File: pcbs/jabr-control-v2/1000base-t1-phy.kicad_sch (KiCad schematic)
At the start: 28 parts, among them J701 MSPE-J2L0-x00, U701 LAN8870, Y701 XRCGB25M000F3A16R0

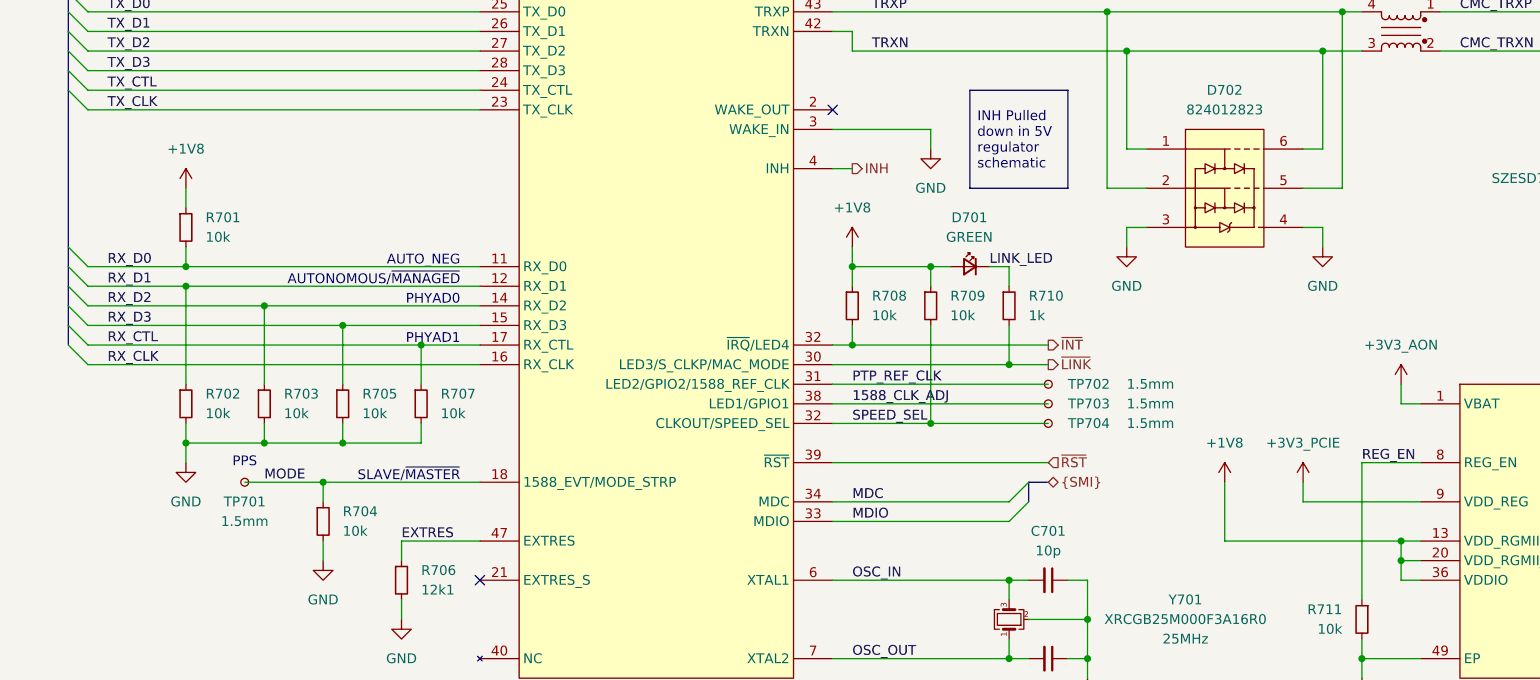
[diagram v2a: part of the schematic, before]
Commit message: PCI11010 IO done
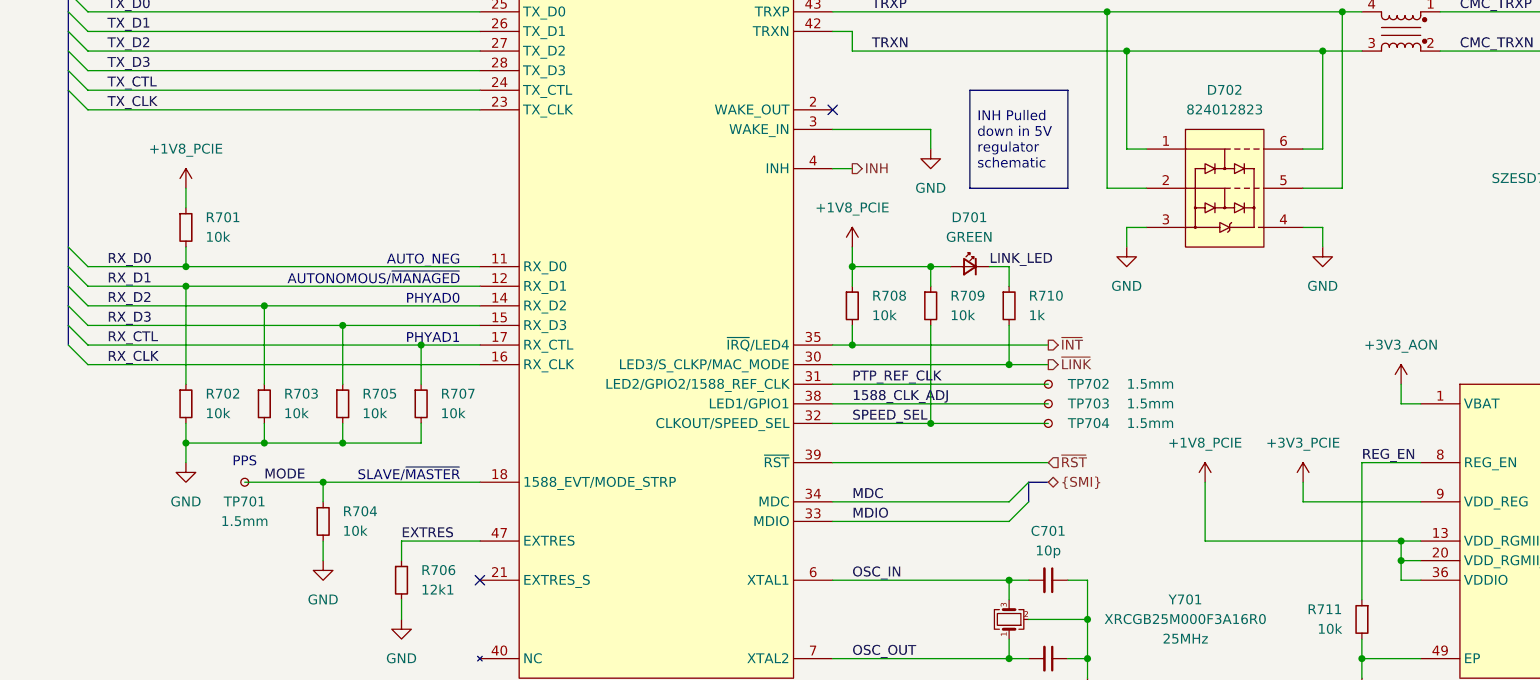
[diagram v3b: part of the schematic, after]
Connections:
- net ~{INT}: now also U701.35 (~{IRQ}/LED4); no longer U701.32 (CLKOUT/SPEED_SEL)
- net +1V8 renamed +1V8_PCIE
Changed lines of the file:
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@@
 	(wire
 		(pts
-			(xy 177.8 121.92) (xy 200.66 121.92)
+			(xy 175.26 121.92) (xy 200.66 121.92)
 		)
 		(stroke
@@
 	(wire
 		(pts
-			(xy 177.8 114.3) (xy 177.8 121.92)
+			(xy 175.26 114.3) (xy 175.26 121.92)
 		)
 		(stroke
@@
 	)
 	(symbol
+		(lib_id "PWR-SYM:+1V8_PCIE")
+		(at 43.18 76.2 0)
+		(unit 1)
+		(body_style 1)
+		(exclude_from_sim no)
+		(in_bom yes)
+		(on_board yes)
+		(in_pos_files yes)
+		(dnp no)
+		(fields_autoplaced yes)
+		(property "Reference" "#PWR0718"
+			(at 43.18 80.01 0)
+			(hide yes)
+			(show_name no)
+			(do_not_autoplace no)
+			(effects
+				(font
+					(size 1.27 1.27)
+				)
+			)
+		)
+		(property "Value" "+1V8_PCIE"
+			(at 43.18 71.12 0)
+			(show_name no)
+			(do_not_autoplace no)
+			(effects
+				(font
+					(size 1.27 1.27)
+				)
+			)
+		)
+		(property "Footprint" ""
+			(at 43.18 76.2 0)
+			(hide yes)
+			(show_name no)
+			(do_not_autoplace no)
+			(effects
+				(font
+					(size 1.27 1.27)
+				)
+			)
+		)
+		(property "Datasheet" ""
+			(at 43.18 76.2 0)
+			(hide yes)
+			(show_name no)
+			(do_not_autoplace no)
+			(effects
+				(font
+					(size 1.27 1.27)
+				)
+			)
+		)
+		(property "Description" "Power symbol creates a global label with name \"+1V8_PCIE\""
+			(at 43.18 76.2 0)
+			(hide yes)
+			(show_name no)
+			(do_not_autoplace no)
+			(effects
+				(font
+					(size 1.27 1.27)
+				)
+			)
+		)
+		(pin "1"
+		)
+		(instances
+			(project "jabr-control-v2"
+				(path "/f91ec272-d09a-4038-bbbb-962739a92c51/760d12ad-9269-4cb7-9058-d98dd001df15"
+					(reference "#PWR0718")
+					(unit 1)
+				)
+			)
+		)
+	)
+	(symbol
 		(lib_id "COMM-CMC:ACT1210G-800-2P-TL10")
 		(at 200.66 53.34 0)
@@
 	)
 	(symbol
-		(lib_id "power:+1V8")
-		(at 177.8 114.3 0)
-		(unit 1)
-		(body_style 1)
-		(exclude_from_sim no)
-		(in_bom yes)
-		(on_board yes)
-		(in_pos_files yes)
-		(dnp no)
-		(fields_autoplaced yes)
-		(property "Reference" "#PWR0709"
-			(at 177.8 118.11 0)
-			(hide yes)
-			(show_name no)
-			(do_not_autoplace no)
-			(effects
-				(font
-					(size 1.27 1.27)
-				)
-			)
-		)
-		(property "Value" "+1V8"
-			(at 177.8 109.22 0)
-			(show_name no)
-			(do_not_autoplace no)
-			(effects
-				(font
-					(size 1.27 1.27)
-				)
-			)
-		)
-		(property "Footprint" ""
-			(at 177.8 114.3 0)
-			(hide yes)
-			(show_name no)
-			(do_not_autoplace no)
-			(effects
-				(font
-					(size 1.27 1.27)
-				)
-			)
-		)
-		(property "Datasheet" ""
-			(at 177.8 114.3 0)
-			(hide yes)
-			(show_name no)
-			(do_not_autoplace no)
-			(effects
-				(font
-					(size 1.27 1.27)
-				)
-			)
-		)
-		(property "Description" "Power symbol creates a global label with name \"+1V8\""
-			(at 177.8 114.3 0)
-			(hide yes)
-			(show_name no)
-			(do_not_autoplace no)
-			(effects
-				(font
-					(size 1.27 1.27)
-				)
-			)
-		)
-		(pin "1"
-		)
-		(instances
-			(project "jabr-control-v2"
-				(path "/f91ec272-d09a-4038-bbbb-962739a92c51/760d12ad-9269-4cb7-9058-d98dd001df15"
-					(reference "#PWR0709")
-					(unit 1)
-				)
-			)
-		)
-	)
-	(symbol
 		(lib_id "DEV:R_SMALL")
 		(at 139.7 91.44 0)
@@
 	)
 	(symbol
-		(lib_id "power:+1V8")
-		(at 129.54 83.82 0)
-		(unit 1)
-		(body_style 1)
-		(exclude_from_sim no)
-		(in_bom yes)
-		(on_board yes)
-		(in_pos_files yes)
-		(dnp no)
-		(fields_autoplaced yes)
-		(property "Reference" "#PWR0705"
-			(at 129.54 87.63 0)
-			(hide yes)
-			(show_name no)
-			(do_not_autoplace no)
-			(effects
-				(font
-					(size 1.27 1.27)
-				)
-			)
-		)
-		(property "Value" "+1V8"
-			(at 129.54 78.74 0)
-			(show_name no)
-			(do_not_autoplace no)
-			(effects
-				(font
-					(size 1.27 1.27)
-				)
-			)
-		)
-		(property "Footprint" ""
-			(at 129.54 83.82 0)
-			(hide yes)
-			(show_name no)
-			(do_not_autoplace no)
-			(effects
-				(font
-					(size 1.27 1.27)
-				)
-			)
-		)
-		(property "Datasheet" ""
-			(at 129.54 83.82 0)
-			(hide yes)
-			(show_name no)
-			(do_not_autoplace no)
-			(effects
-				(font
-					(size 1.27 1.27)
-				)
-			)
-		)
-		(property "Description" "Power symbol creates a global label with name \"+1V8\""
-			(at 129.54 83.82 0)
-			(hide yes)
-			(show_name no)
-			(do_not_autoplace no)
-			(effects
-				(font
-					(size 1.27 1.27)
-				)
-			)
-		)
-		(pin "1"
-		)
-		(instances
-			(project "jabr-control-v2"
-				(path "/f91ec272-d09a-4038-bbbb-962739a92c51/760d12ad-9269-4cb7-9058-d98dd001df15"
-					(reference "#PWR0705")
-					(unit 1)
-				)
-			)
-		)
-	)
-	(symbol
 		(lib_id "power:GND")
 		(at 160.02 139.7 0)
@@
 	)
 	(symbol
-		(lib_id "power:+1V8")
-		(at 43.18 76.2 0)
+		(lib_id "PWR-SYM:+1V8_PCIE")
+		(at 129.54 83.82 0)
 		(unit 1)
 		(body_style 1)
@@
 		(dnp no)
 		(fields_autoplaced yes)
-		(property "Reference" "#PWR0701"
-			(at 43.18 80.01 0)
+		(property "Reference" "#PWR0716"
+			(at 129.54 87.63 0)
 			(hide yes)
 			(show_name no)
@@
 			)
 		)
-		(property "Value" "+1V8"
-			(at 43.18 71.12 0)
+		(property "Value" "+1V8_PCIE"
+			(at 129.54 78.74 0)
 			(show_name no)
 			(do_not_autoplace no)
@@
 		)
 		(property "Footprint" ""
-			(at 43.18 76.2 0)
+			(at 129.54 83.82 0)
 			(hide yes)
 			(show_name no)
@@
 		)
 		(property "Datasheet" ""
-			(at 43.18 76.2 0)
+			(at 129.54 83.82 0)
 			(hide yes)
 			(show_name no)
@@
 			)
 		)
-		(property "Description" "Power symbol creates a global label with name \"+1V8\""
-			(at 43.18 76.2 0)
+		(property "Description" "Power symbol creates a global label with name \"+1V8_PCIE\""
+			(at 129.54 83.82 0)
 			(hide yes)
 			(show_name no)
@@
 			(project "jabr-control-v2"
 				(path "/f91ec272-d09a-4038-bbbb-962739a92c51/760d12ad-9269-4cb7-9058-d98dd001df15"
-					(reference "#PWR0701")
+					(reference "#PWR0716")
 					(unit 1)
 				)
@@
 		)
 		(property "Footprint" "project_footprints:lan8870"
-			(at 104.14 149.86 0)
+			(at 104.14 142.24 0)
 			(hide yes)
 			(show_name no)
@@
 		)
 		(property "Datasheet" "https://ww1.microchip.com/downloads/aemDocuments/documents/UNG/ProductDocuments/ProductBrief/LAN8870-LAN8871-LAN8872-Product-Brief-DS00004469.pdf"
-			(at 104.14 157.48 0)
+			(at 104.14 149.86 0)
 			(hide yes)
 			(show_name no)
@@
 		)
 		(property "Description" "100/1000BASE-T1 PHY"
-			(at 104.14 153.67 0)
+			(at 104.14 146.05 0)
 			(hide yes)
 			(show_name no)
@@
 		(pin "32"
 		)
-		(pin "32"
+		(pin "35"
 		)
 		(pin "34"
@@
 					(unit 1)
 				)
+			)
+		)
+	)
+	(symbol
+		(lib_id "PWR-SYM:+1V8_PCIE")
+		(at 175.26 114.3 0)
+		(unit 1)
+		(body_style 1)
+		(exclude_from_sim no)
+		(in_bom yes)
+		(on_board yes)
+		(in_pos_files yes)
+		(dnp no)
+		(fields_autoplaced yes)
+		(property "Reference" "#PWR0721"
+			(at 175.26 118.11 0)
+			(hide yes)
+			(show_name no)
+			(do_not_autoplace no)
+			(effects
+				(font
+					(size 1.27 1.27)
+				)
+			)
+		)
+		(property "Value" "+1V8_PCIE"
+			(at 175.26 109.22 0)
+			(show_name no)
+			(do_not_autoplace no)
+			(effects
+				(font
+					(size 1.27 1.27)
+				)
+			)
+		)
+		(property "Footprint" ""
+			(at 175.26 114.3 0)
+			(hide yes)
+			(show_name no)
+			(do_not_autoplace no)
+			(effects
+				(font
+					(size 1.27 1.27)
+				)
+			)
+		)
+		(property "Datasheet" ""
+			(at 175.26 114.3 0)
+			(hide yes)
+			(show_name no)
+			(do_not_autoplace no)
+			(effects
+				(font
+					(size 1.27 1.27)
+				)
+			)
+		)
+		(property "Description" "Power symbol creates a global label with name \"+1V8_PCIE\""
+			(at 175.26 114.3 0)
+			(hide yes)
+			(show_name no)
+			(do_not_autoplace no)
+			(effects
+				(font
+					(size 1.27 1.27)
+				)
+			)
+		)
+		(pin "1"
+		)
+		(instances
+			(project "jabr-control-v2"
+				(path "/f91ec272-d09a-4038-bbbb-962739a92c51/760d12ad-9269-4cb7-9058-d98dd001df15"
+					(reference "#PWR0721")
+					(unit 1)
+				)

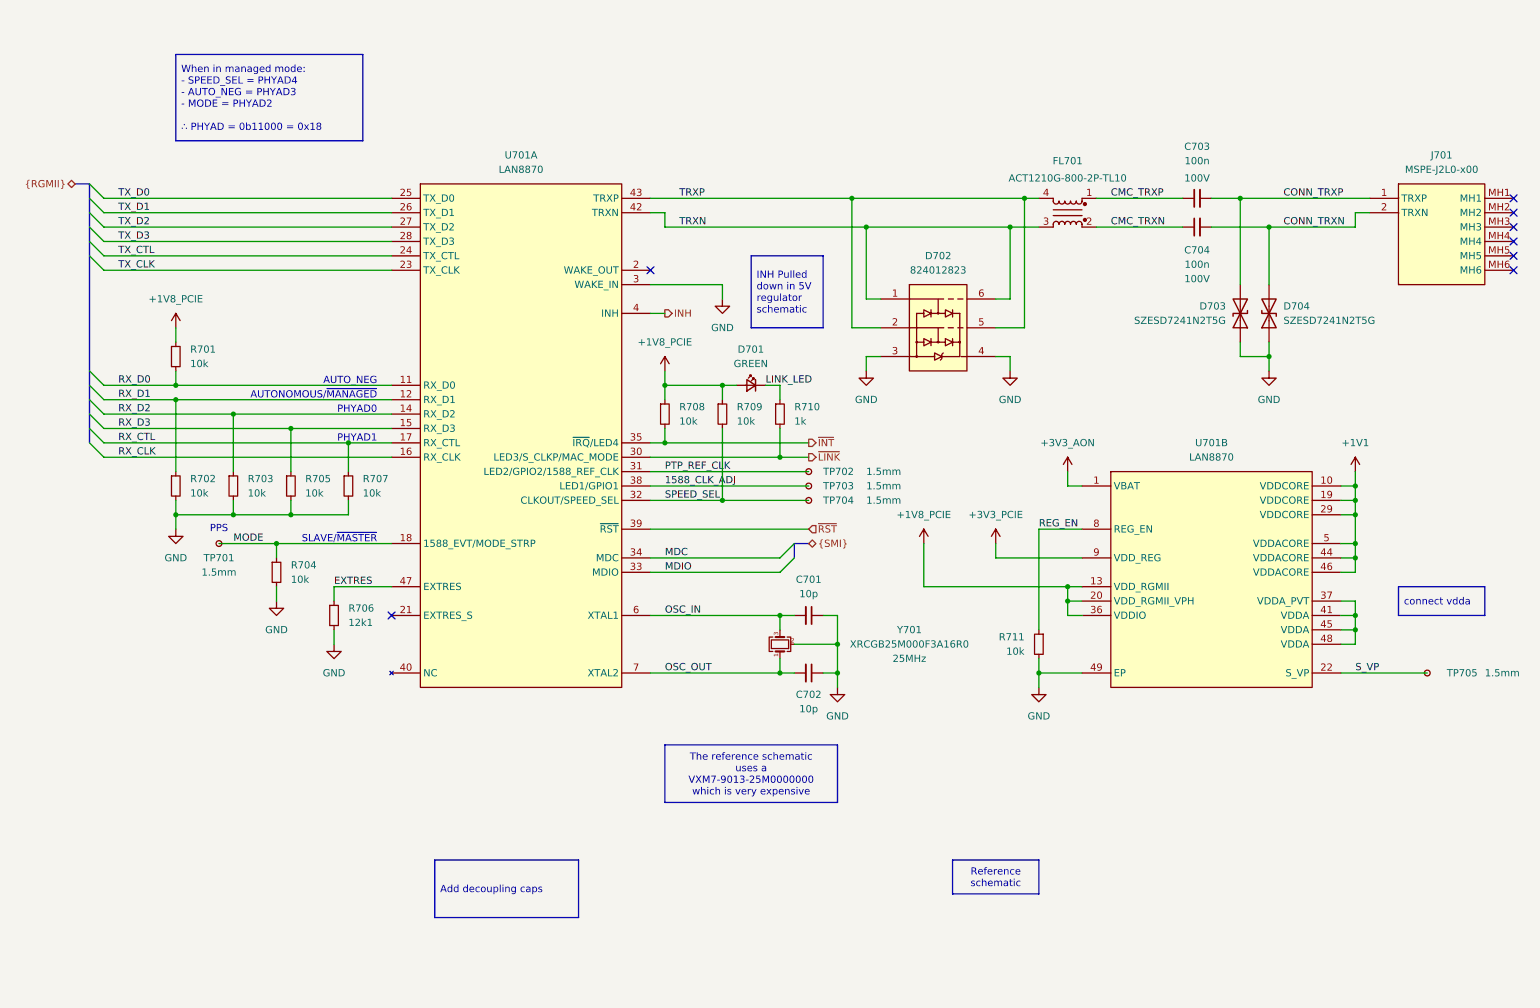
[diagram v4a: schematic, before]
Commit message: Schematic done
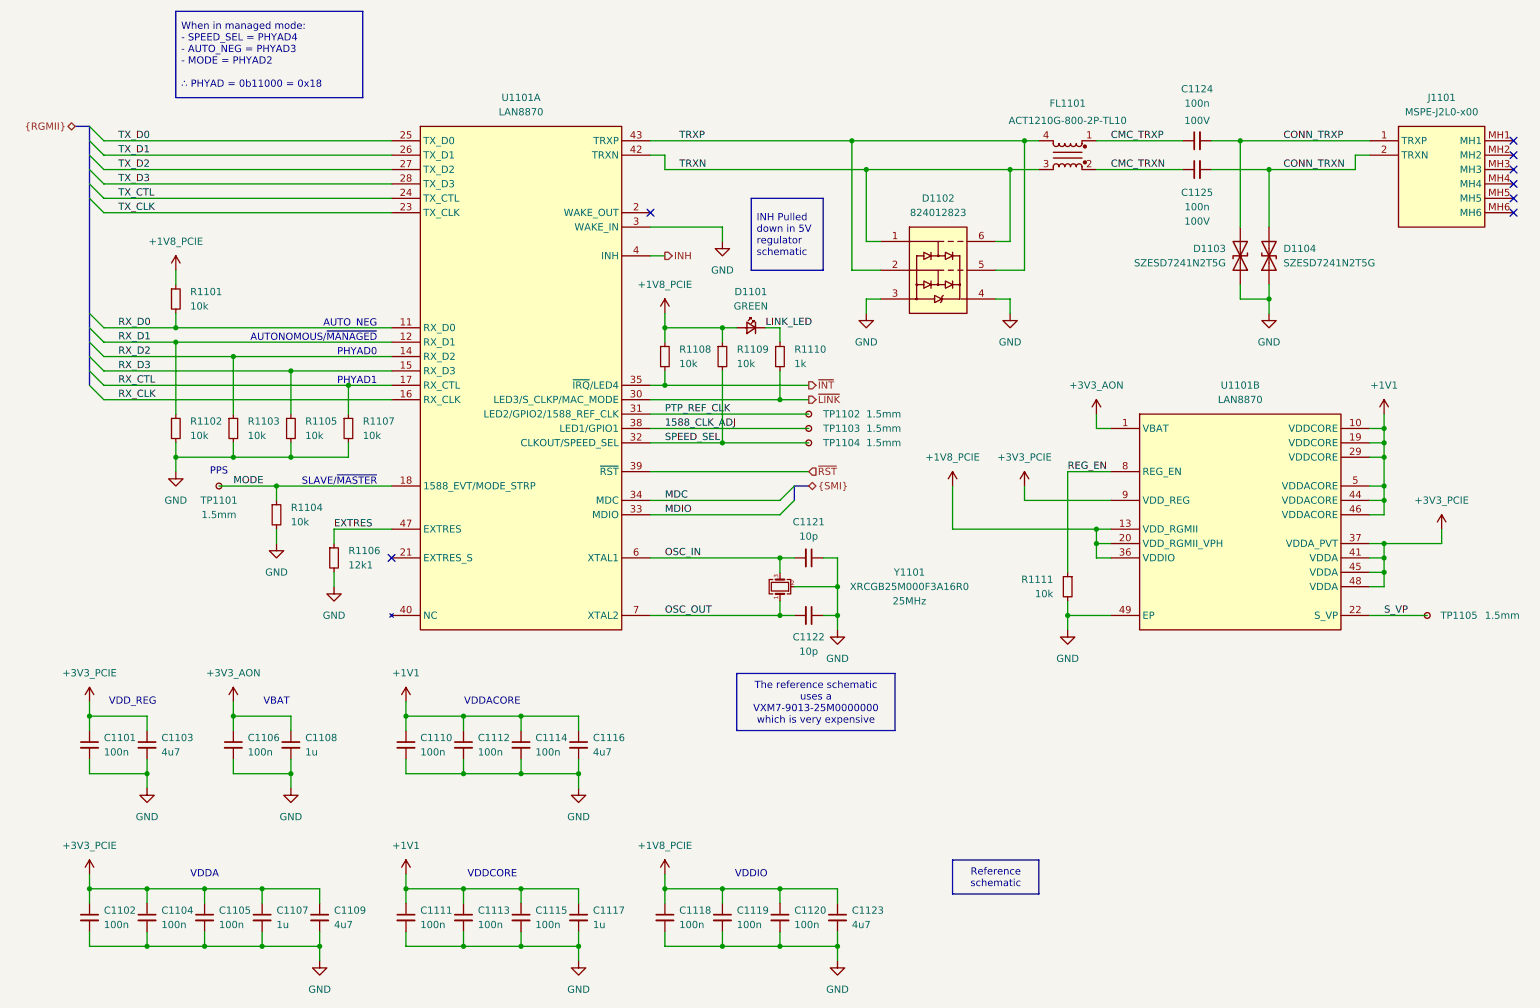
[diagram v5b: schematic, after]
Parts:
- added C1101, C1102, C1104, C1105, C1106, C1110, C1111, C1112, C1113, C1114, C1115, C1118, C1119, C1120: 100n, project_footprints:C_0402, symbol DEV:C_SMALL
- added C1103, C1109, C1116, C1123: 4u7, project_footprints:C_0402, symbol DEV:C_SMALL
- added C1107, C1108, C1117: 1u, project_footprints:C_0402, symbol DEV:C_SMALL
- renumbered C701 to C1121, C702 to C1122, C703 to C1124, C704 to C1125, D701 to D1101, D702 to D1102, D703 to D1103, D704 to D1104, FL701 to FL1101, J701 to J1101, R701 to R1101, R702 to R1102, R703 to R1103, R704 to R1104, R705 to R1105, R706 to R1106, R707 to R1107, R708 to R1108, R709 to R1109, R710 to R1110, R711 to R1111, TP701 to TP1101, TP702 to TP1102, TP703 to TP1103, TP704 to TP1104, TP705 to TP1105, U701 to U1101, Y701 to Y1101
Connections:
- net +1V1: now also C1110.1, C1111.1, C1112.1, C1113.1, C1114.1, C1115.1, C1116.1, C1117.1
- net +1V8_PCIE: now also C1118.1, C1119.1, C1120.1, C1123.1
- net +3V3_AON: now also C1106.1, C1108.1
- net +3V3_PCIE: now also U1101.37 (VDDA_PVT), U1101.41 (VDDA), U1101.45 (VDDA), U1101.48 (VDDA), C1101.1, C1102.1, C1103.1, C1104.1, C1105.1, C1107.1, C1109.1
- net GND: now also C1101.2, C1102.2, C1103.2, C1104.2, C1105.2, C1106.2, C1107.2, C1108.2, C1109.2, C1110.2, C1111.2, C1112.2, C1113.2, C1114.2, C1115.2, C1116.2, C1117.2, C1118.2, C1119.2, C1120.2, C1123.2
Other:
- note added: "VBAT"
- note added: "VDDA"
- note added: "VDDACORE"
- note added: "VDDCORE"
- note added: "VDDIO"
- note added: "VDD_REG"
- moved on the sheet: C1121, C1122, C1124, C1125, D1101, D1102, D1103, D1104, FL1101, J1101, R1101, R1102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
